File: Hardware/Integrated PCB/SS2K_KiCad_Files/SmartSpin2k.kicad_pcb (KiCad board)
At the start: 2 copper layers, 57.2 x 60.3 mm, 88 parts, among them J1 B4B-XH-AMLFSN, J2 B8B-XH-A_LFSN, J3 10118194-0001LF, J4 B4B-XH-AMLFSN, Q1 S8050, Q2 S8050, Q3 S8050, Q4 S8050, SW1 SW_Push, SW4 SW_Push, U1 TMC2209-LA-T, U2 TPS5430DDA, U3 ESP32-WROOM-32D, U4 INTERFACE-CP2102-GMR(QFN28), U5 MAX3232, U6 LM1117-3.3

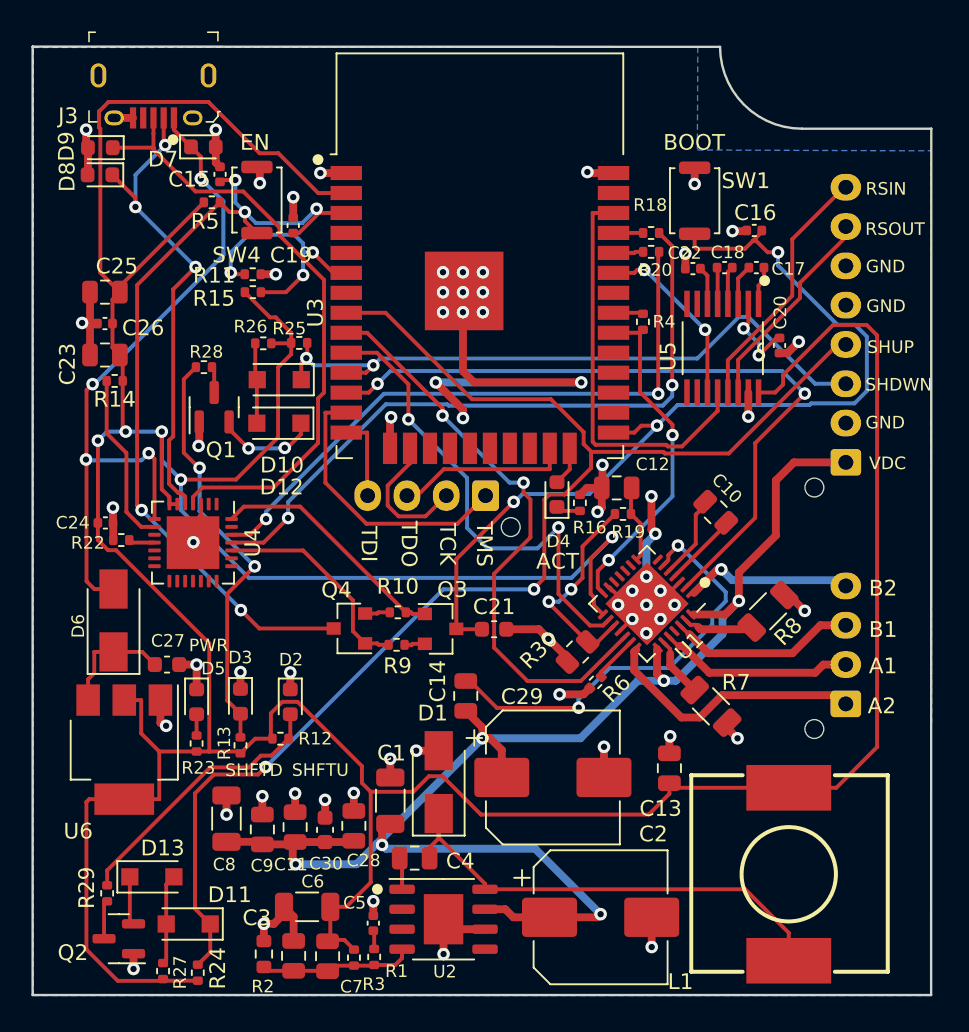
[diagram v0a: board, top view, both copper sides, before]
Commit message: PCB Switch Added and LEDs moved
- Added SMD Switch near top of PCB to protrude outside of the case for Peloton bikes.
- Moved LEDs in order to allow for possible future "Light tubes" to show status of board outside of the case.
- Added Logos
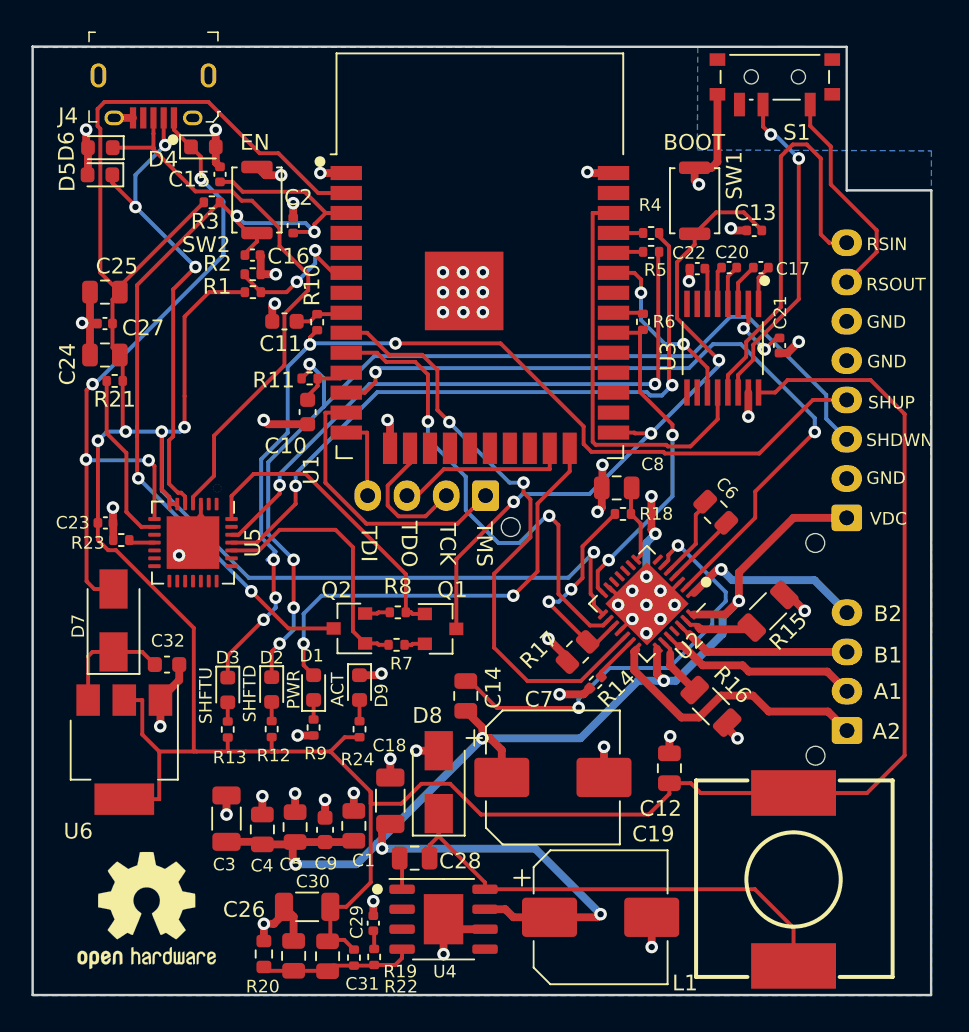
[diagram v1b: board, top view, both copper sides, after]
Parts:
- removed the C21 at (150.7, 125.7)
- removed D10, D11, D12, D13: D, Diode_SMD:D_SOD-123F
- removed the Q1 at (132.9, 111.6)
- removed the Q2 at (126.8, 145.4)
- removed the R12 at (137.1, 132.7)
- removed R25, R26, R27: 4.7k, Resistor_SMD:R_0402_1005Metric
- removed R28, R29: 200, Resistor_SMD:R_0402_1005Metric
- added C10: 1uF, Capacitor_SMD:C_0603_1608Metric, F.Cu at (138.8, 111.9)
- added C11: 1uF, Capacitor_SMD:C_0603_1608Metric, F.Cu at (137.3, 106.1)
- added C16: 2.2uF, Capacitor_SMD:C_0402_1005Metric, F.Cu at (135.3, 101.9)
- added G***: LOGO, IEEE_Logo:SS2K_QR_Code_25x25mm, B.Cu at (149.7, 100.0)
- added G***: LOGO, IEEE_Logo:SmartSpin_ScreenPrint_One_25x25mm, B.Cu at (133.6, 136.7)
- added R10: 200, Resistor_SMD:R_0402_1005Metric, F.Cu at (139.4, 106.2)
- added R11: 200, Resistor_SMD:R_0402_1005Metric, F.Cu at (138.9, 109.8)
- added REF**: OSHW-Logo2_9.8x8mm_SilkScreen, Symbol:OSHW-Logo2_9.8x8mm_SilkScreen, F.Cu at (128.6, 143.6)
- added S1: EG1218, Button_Switch_SMD:SW_SPDT_PCM12, F.Cu at (168.5, 90.9)
- R13: renamed from R24; value 4.7k -> 330
- moved R9 22.2 mm to (139.2, 132.0), turned to 90 degrees
- moved D1 19.8 mm to (139.2, 129.4)
- moved R13 15.6 mm to (133.7, 132.1), turned to 90 degrees
- moved R24 10.4 mm to (142.1, 132.1)
- moved D9 10.4 mm to (142.1, 129.4)
- moved D3 4.05 mm to (133.7, 129.6)
- moved J3 3.53 mm to (173.1, 118.6)
- moved R12 2.24 mm to (136.5, 132.1)
- moved D2 2.12 mm to (136.5, 129.5)
- moved J1 1.70 mm to (173.1, 132.1)
- moved L1 0.45 mm to (162.1, 141.6)
- moved C20 0.28 mm to (165.6, 102.7)
- moved C22 0.28 mm to (163.6, 102.8)
- moved C17 0.28 mm to (167.6, 102.7)
- renumbered C28 to C1, C13 to C12, C16 to C13, C1 to C18, C2 to C19, C19 to C2, C18 to C20, C20 to C21, C24 to C23, C23 to C24, C3 to C26, C26 to C27, C4 to C28, C5 to C29, C8 to C3, C6 to C30, C7 to C31, C27 to C32, C9 to C4, C11 to C5, C10 to C6, C29 to C7, C12 to C8, C30 to C9, D4 to D1, D3 to D2, D2 to D3, D7 to D4, D8 to D5, D9 to D6, D6 to D7, D1 to D8, D5 to D9, J4 to J2, J2 to J3, J3 to J4, Q3 to Q1, Q4 to Q2, R15 to R1, R13 to R12, R6 to R14, R8 to R15, R7 to R16, R30 to R17, R19 to R18, R1 to R19, R11 to R2, R2 to R20, R14 to R21, R3 to R22, R22 to R23, R23 to R24, R5 to R3, R18 to R4, R20 to R5, R4 to R6, R9 to R7, R10 to R8, R16 to R9, SW4 to SW2, U3 to U1, U1 to U2, U5 to U3, U2 to U4, U4 to U5
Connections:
- D2 pad 1: GND -> /ShiftDown
- D3 pad 1: GND -> /ShiftUp
- D3 pad 2: Net-(D2-Pad2) (its old number) -> Net-(D3-Pad2)
- R13 pad 1: /ShiftUp -> /3V3
- R13 pad 2: /3V3 -> Net-(D3-Pad2)
- U1 pad 11: /ShiftDown -> Net-(C10-Pad1)
- U1 pad 8: /ShiftUp -> Net-(C11-Pad1)
- U3 pad 14: /RS232OUT1 -> Net-(S1-Pad2)
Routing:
- net /3V3: track 275.7 -> 244.3 mm
- net Net-(D1-Pad2): track 2.49 -> 28.8 mm, vias 0 -> 2
- net Net-(D2-Pad2): track 26.8 -> 1.22 mm, vias 2 -> 0
- net /ShiftUp: track 88.2 -> 65.0 mm, vias 2 -> 5
- net /ShiftDown: track 41.9 -> 63.9 mm, vias 2 -> 4
- net Net-(S1-Pad2): track 0.00 -> 21.0 mm, vias 0 -> 2
- net Net-(D2-Pad2) (its old number): track 17.6 -> 0.00 mm
- net GND: track 113.1 -> 96.4 mm, vias 64 -> 60
- net /IO0_BOOT: track 59.0 -> 43.9 mm
- net /RS232IN1: track 16.2 -> 26.3 mm
- net Net-(R1-Pad2): track 16.6 -> 9.36 mm, vias 3 -> 2
- net Net-(D12-Pad1): track 6.60 -> 0.00 mm, vias 2 -> 0
- net /EN: track 53.5 -> 59.6 mm, vias 5 -> 4
- net Net-(D11-Pad2): track 5.77 -> 0.00 mm
- net Net-(D10-Pad2): track 5.14 -> 0.00 mm
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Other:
- outline, holes or cut-outs redrawn
- board text added: "Rev. 2.4"
- board text removed: "Rev. 2.121"
